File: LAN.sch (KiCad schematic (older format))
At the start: 34 parts, among them J1 Pulse_JXD6-0001NL, U7 LAN8742A-CZ-TR, Y1 NX2016SA-25MHz

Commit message: begin MCU editing
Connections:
- net RMII_CRS_DV: no longer R13.1, R14.1
- new net RMII_RXD0: R13.1
- new net RMII_RXD1: R14.1
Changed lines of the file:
@@
 $Descr A4 11693 8268
 encoding utf-8
-Sheet 2 10
+Sheet 2 9
 Title ""
 Date ""
@@
 Wire Wire Line
 	1130 3590 1380 3590
-Text HLabel 1130 3590 0    50   BiDi ~ 0
-RMII_CRS_DV
 Wire Wire Line
 	1680 3590 2410 3590
@@
 Wire Wire Line
 	1130 3490 1380 3490
-Text HLabel 1130 3490 0    50   BiDi ~ 0
-RMII_CRS_DV
 Wire Wire Line
 	1680 3490 2130 3490
@@
 Wire Wire Line
 	10120 2490 10120 2590
+Text HLabel 1130 3490 0    50   BiDi ~ 0
+RMII_RXD0
+Text HLabel 1130 3590 0    50   BiDi ~ 0
+RMII_RXD1
 $EndSCHEMATC

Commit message: v0.1
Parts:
- added J11: OSTTC020162, digikey-footprints:Term_Block_1x2_P5mm, symbol dk_Terminal-Blocks-Wire-to-Board:OSTTC020162
- renumbered C6 to C86, C7 to C87, C8 to C88, C9 to C89, C10 to C90, C11 to C91, C12 to C92, C13 to C93, C14 to C94, C15 to C95, C16 to C96, D1 to D13, J1 to J10, L2 to L6, R1 to R74, R2 to R75, R3 to R76, R4 to R77, R5 to R78, R6 to R79, R7 to R80, R8 to R81, R9 to R82, R10 to R83, R11 to R84, R12 to R85, R13 to R86, R14 to R87, R15 to R88, R16 to R89, R17 to R90, R18 to R91, U7 to U28, Y1 to Y3
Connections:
- net GNDS: now also J11.1, J11.2

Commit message: v0.3 changed sd_card holder
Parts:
- renumbered C86 to C83, C87 to C84, C88 to C85, C89 to C86, C90 to C87, C91 to C88, C92 to C89, C93 to C90, C94 to C91, C95 to C92, C96 to C93, D13 to D15, J10 to J11, J11 to J12, R74 to R78, R75 to R79, R76 to R80, R77 to R81, R78 to R82, R79 to R83, R80 to R84, R81 to R85, R82 to R86, R83 to R87, R84 to R88, R85 to R89, R86 to R90, R87 to R91, R88 to R92, R89 to R93, R90 to R94, R91 to R95, U28 to U30

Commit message: footprints associations is done
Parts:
- C94: renamed from C92; Type CL10B105KA8NNNC -> GRM188R71H471KA01D
- D15: footprint digikey-footprints:SOT23-6L -> Package_TO_SOT_SMD:SOT-23-6_Handsoldering
- L6: value 600R@100MHz -> 600R@100MHz [BK2125HS601-T]; footprint (none) -> Inductor_SMD:L_0805_2012Metric_Pad1.15x1.40mm_HandSolder
- Y3: footprint (none) -> Crystal:Crystal_SMD_2016-4Pin_2.0x1.6mm
- renumbered C83 to C85, C84 to C86, C85 to C87, C86 to C88, C87 to C89, C88 to C90, C89 to C91, C90 to C92, C91 to C93, C93 to C95, R92 to R100, R93 to R101, R94 to R102, R95 to R103, R78 to R86, R79 to R87, R80 to R88, R81 to R89, R82 to R90, R83 to R91, R84 to R92, R85 to R93, R86 to R94, R87 to R95, R88 to R96, R89 to R97, R90 to R98, R91 to R99
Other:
- moved on the sheet: J12

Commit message: LAN8742 footprint corrected
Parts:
- U30: footprint LAN8742:Microchip-C04-143B-S4QFN-0-0-* -> SVIELCOM:Microchip-C04-143B-S4QFN-0-0-IPC_A
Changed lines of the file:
@@
 F 0 "U30" H 4790 3535 50  0000 C CNN
 F 1 "LAN8742A-CZ-TR" H 4790 3444 50  0000 C CNN
-F 2 "LAN8742:Microchip-C04-143B-S4QFN-0-0-*" H 3290 3670 50  0001 L CNN
+F 2 "SVIELCOM:Microchip-C04-143B-S4QFN-0-0-IPC_A" H 3290 3670 50  0001 L CNN
 F 3 "http://ww1.microchip.com/downloads/en/DeviceDoc/DS_LAN8742_00001989A.pdf" H 3290 3770 50  0001 L CNN
 F 4 "+70°C" H 3290 3870 50  0001 L CNN "ambient temperature range high"

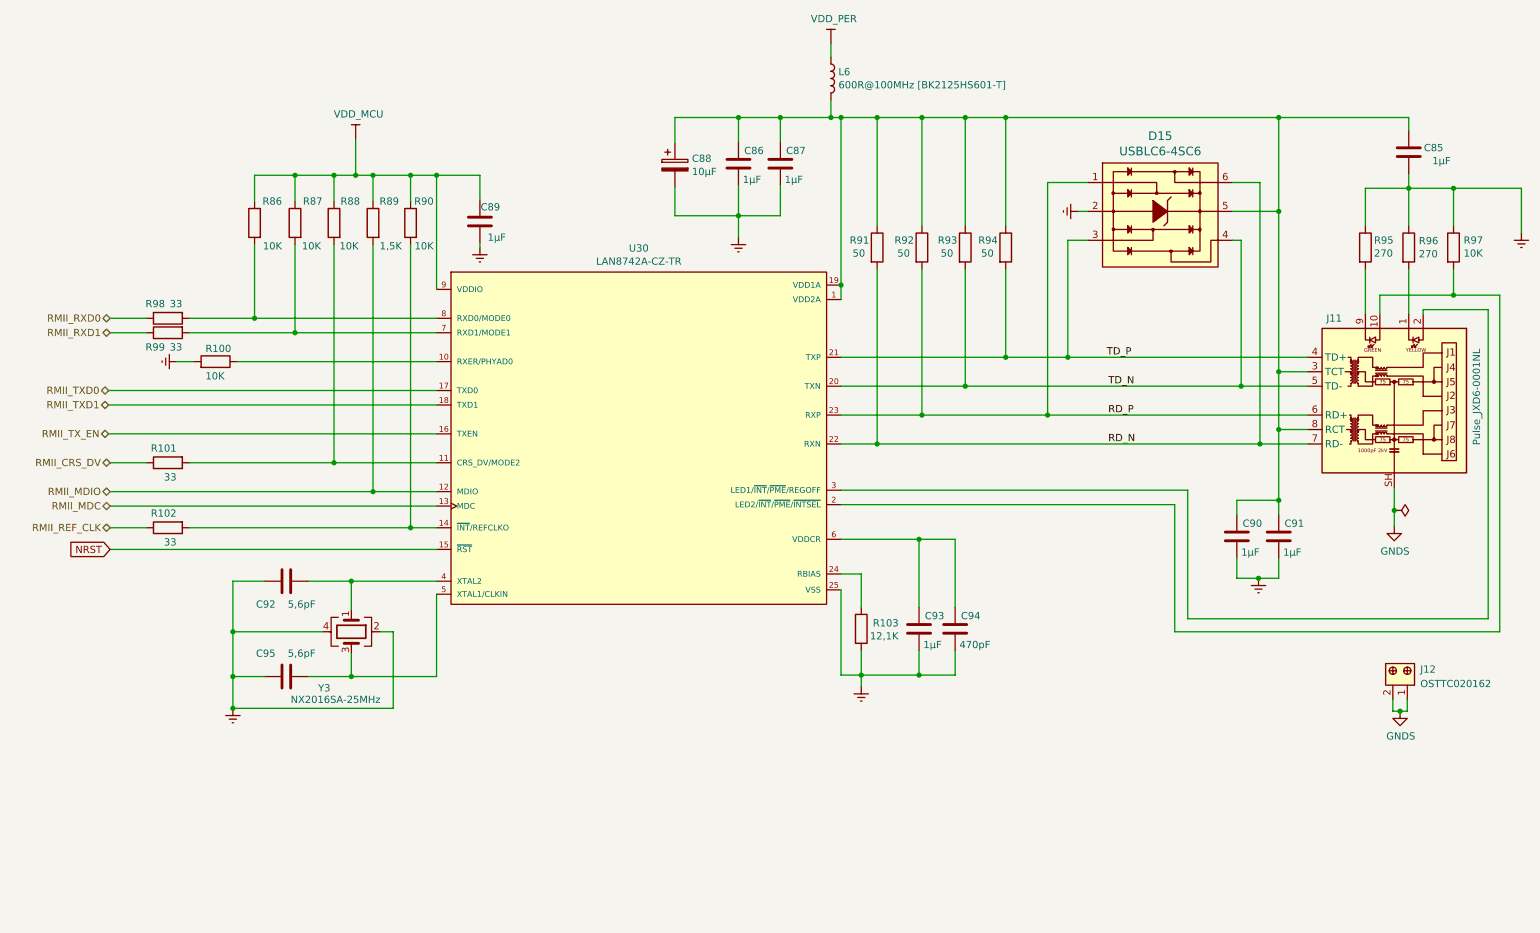
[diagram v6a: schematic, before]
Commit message: corrected few footprints, correct all resistors and capacitors type for ordering
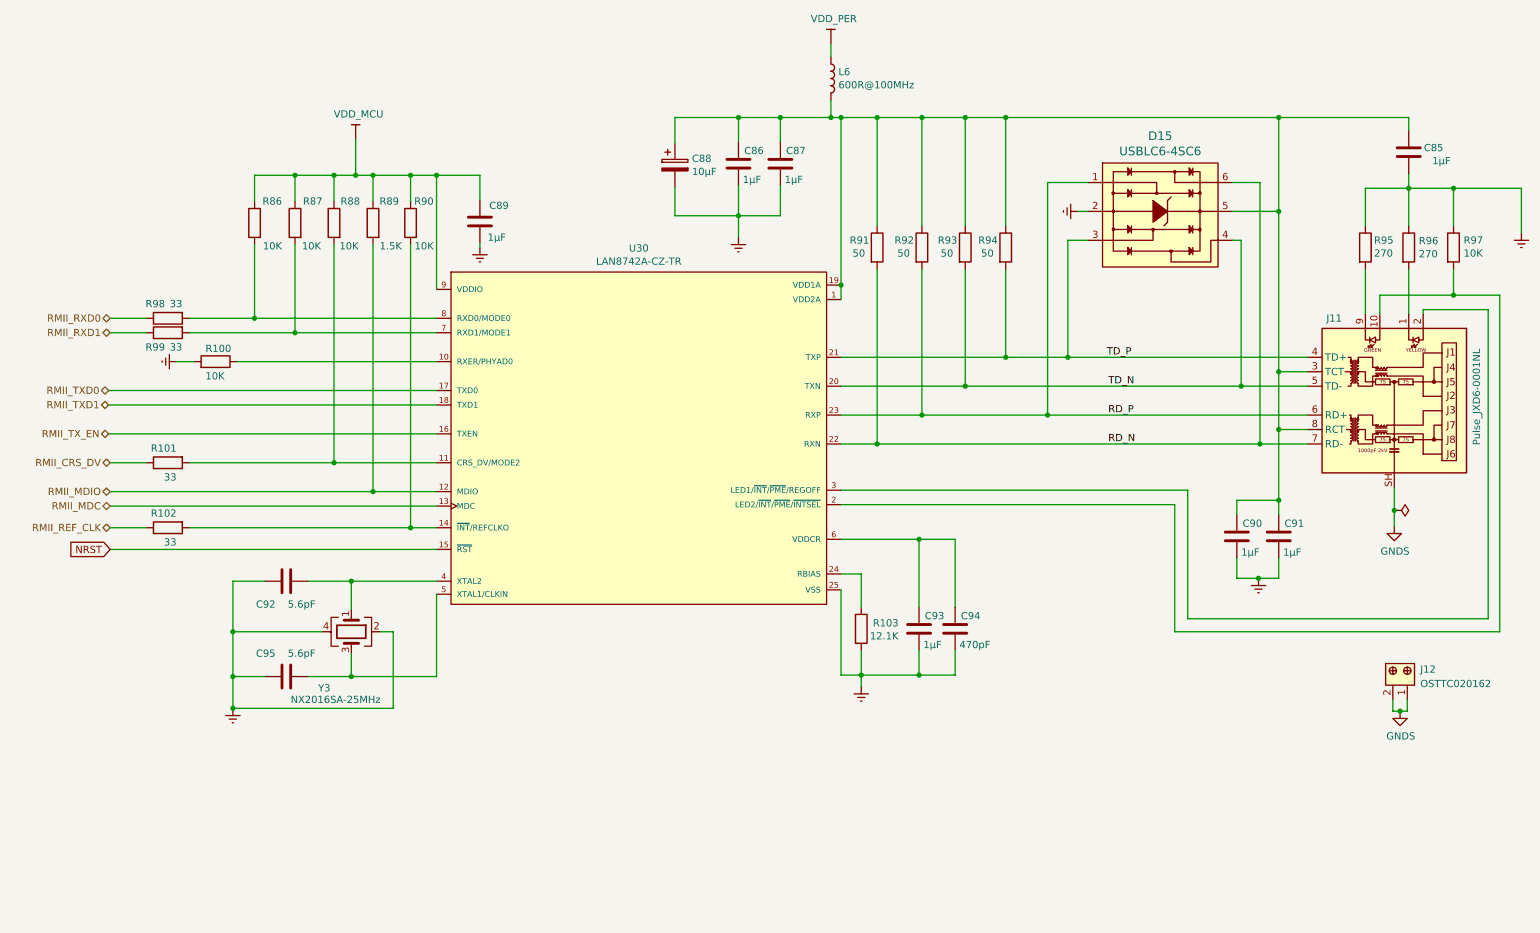
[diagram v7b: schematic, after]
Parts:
- C92, C95: value 5,6pF -> 5.6pF; Type CL10B105KA8NNNC -> CC0603CRNPO9BN5R6
- L6: value 600R@100MHz [BK2125HS601-T] -> 600R@100MHz; Type (none) -> BK2125HS601-T
- R100, R86, R87, R88, R90, R97: Type (none) -> RC0805FR-0710KL
- R101, R102, R98, R99: Type (none) -> RC0805FR-0733RL
- R103: value 12,1K -> 12.1K; Type (none) -> RC0805FR-0712K1L
- R89: value 1,5K -> 1.5K; Type (none) -> RC0805FR-071K5L
- R91, R92, R93, R94: footprint Resistor_SMD:R_0805_2012Metric_Pad1.20x1.40mm_HandSolder -> Resistor_SMD:R_0603_1608Metric_Pad0.98x0.95mm_HandSolder; Type (none) -> CRCW060350R0FKEA
- R95, R96: Type (none) -> RC0805FR-07270RL
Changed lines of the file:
@@
 F 2 "Resistor_SMD:R_0805_2012Metric_Pad1.20x1.40mm_HandSolder" V 10360 3000 50  0001 C CNN
 F 3 "~" H 10430 3000 50  0001 C CNN
+F 4 "RC0805FR-0710KL" H 10430 3000 50  0001 C CNN "Type"
 	1    10430 3000
 	1    0    0    -1
@@
 F 2 "Resistor_SMD:R_0805_2012Metric_Pad1.20x1.40mm_HandSolder" V 10050 3000 50  0001 C CNN
 F 3 "~" H 10120 3000 50  0001 C CNN
+F 4 "RC0805FR-07270RL" H 10120 3000 50  0001 C CNN "Type"
 	1    10120 3000
 	1    0    0    -1
@@
 F 2 "Resistor_SMD:R_0805_2012Metric_Pad1.20x1.40mm_HandSolder" V 9750 3000 50  0001 C CNN
 F 3 "~" H 9820 3000 50  0001 C CNN
+F 4 "RC0805FR-07270RL" H 9820 3000 50  0001 C CNN "Type"
 	1    9820 3000
 	1    0    0    -1
@@
 F 0 "R94" H 7140 3050 50  0000 L CNN
 F 1 "50" H 7160 2960 50  0000 L CNN
-F 2 "Resistor_SMD:R_0805_2012Metric_Pad1.20x1.40mm_HandSolder" V 7260 3000 50  0001 C CNN
+F 2 "Resistor_SMD:R_0603_1608Metric_Pad0.98x0.95mm_HandSolder" V 7260 3000 50  0001 C CNN
 F 3 "~" H 7330 3000 50  0001 C CNN
+F 4 "CRCW060350R0FKEA" H 7330 3000 50  0001 C CNN "Type"
 	1    7330 3000
 	1    0    0    -1
@@
 F 0 "R93" H 6860 3050 50  0000 L CNN
 F 1 "50" H 6880 2960 50  0000 L CNN
-F 2 "Resistor_SMD:R_0805_2012Metric_Pad1.20x1.40mm_HandSolder" V 6980 3000 50  0001 C CNN
+F 2 "Resistor_SMD:R_0603_1608Metric_Pad0.98x0.95mm_HandSolder" V 6980 3000 50  0001 C CNN
 F 3 "~" H 7050 3000 50  0001 C CNN
+F 4 "CRCW060350R0FKEA" H 7050 3000 50  0001 C CNN "Type"
 	1    7050 3000
 	1    0    0    -1
@@
 F 0 "R92" H 6560 3050 50  0000 L CNN
 F 1 "50" H 6580 2960 50  0000 L CNN
-F 2 "Resistor_SMD:R_0805_2012Metric_Pad1.20x1.40mm_HandSolder" V 6680 3000 50  0001 C CNN
+F 2 "Resistor_SMD:R_0603_1608Metric_Pad0.98x0.95mm_HandSolder" V 6680 3000 50  0001 C CNN
 F 3 "~" H 6750 3000 50  0001 C CNN
+F 4 "CRCW060350R0FKEA" H 6750 3000 50  0001 C CNN "Type"
 	1    6750 3000
 	1    0    0    -1
@@
 F 0 "R91" H 6250 3050 50  0000 L CNN
 F 1 "50" H 6270 2960 50  0000 L CNN
-F 2 "Resistor_SMD:R_0805_2012Metric_Pad1.20x1.40mm_HandSolder" V 6370 3000 50  0001 C CNN
+F 2 "Resistor_SMD:R_0603_1608Metric_Pad0.98x0.95mm_HandSolder" V 6370 3000 50  0001 C CNN
 F 3 "~" H 6440 3000 50  0001 C CNN
+F 4 "CRCW060350R0FKEA" H 6440 3000 50  0001 C CNN "Type"
 	1    6440 3000
 	1    0    0    -1
@@
 P 6330 5640
 F 0 "R103" H 6410 5680 50  0000 L CNN
-F 1 "12,1K" H 6390 5590 50  0000 L CNN
+F 1 "12.1K" H 6390 5590 50  0000 L CNN
 F 2 "Resistor_SMD:R_0805_2012Metric_Pad1.20x1.40mm_HandSolder" V 6260 5640 50  0001 C CNN
 F 3 "~" H 6330 5640 50  0001 C CNN
+F 4 "RC0805FR-0712K1L" H 6330 5640 50  0001 C CNN "Type"
 	1    6330 5640
 	1    0    0    -1
@@
 AR Path="/608C7842/6098C4C6" Ref="C95"  Part="1"
 F 0 "C95" V 2190 5760 50  0000 L CNN
-F 1 "5,6pF" V 2190 5980 50  0000 L CNN
+F 1 "5.6pF" V 2190 5980 50  0000 L CNN
 F 2 "Capacitor_SMD:C_0603_1608Metric_Pad1.08x0.95mm_HandSolder" H 2388 5820 50  0001 C CNN
 F 3 "http://www.farnell.com/datasheets/2710676.pdf" H 2350 5970 50  0001 C CNN
-F 4 "CL10B105KA8NNNC" H 2350 5970 50  0001 C CNN "Type"
+F 4 "CC0603CRNPO9BN5R6" H 2350 5970 50  0001 C CNN "Type"
 	1    2350 5970
 	0    1    1    0
@@
 AR Path="/608C7842/6098D1AF" Ref="C92"  Part="1"
 F 0 "C92" V 2510 5100 50  0000 L CNN
-F 1 "5,6pF" V 2510 5320 50  0000 L CNN
+F 1 "5.6pF" V 2510 5320 50  0000 L CNN
 F 2 "Capacitor_SMD:C_0603_1608Metric_Pad1.08x0.95mm_HandSolder" H 2388 5160 50  0001 C CNN
 F 3 "http://www.farnell.com/datasheets/2710676.pdf" H 2350 5310 50  0001 C CNN
-F 4 "CL10B105KA8NNNC" H 2350 5310 50  0001 C CNN "Type"
+F 4 "CC0603CRNPO9BN5R6" H 2350 5310 50  0001 C CNN "Type"
 	1    2350 5310
 	0    1    1    0
@@
 F 2 "Resistor_SMD:R_0805_2012Metric_Pad1.20x1.40mm_HandSolder" V 3140 2830 50  0001 C CNN
 F 3 "~" H 3210 2830 50  0001 C CNN
+F 4 "RC0805FR-0710KL" H 3210 2830 50  0001 C CNN "Type"
 	1    3210 2830
 	-1   0    0    -1
@@
 F 2 "Resistor_SMD:R_0805_2012Metric_Pad1.20x1.40mm_HandSolder" V 1460 4940 50  0001 C CNN
 F 3 "~" H 1530 4940 50  0001 C CNN
+F 4 "RC0805FR-0733RL" V 1530 4940 50  0001 C CNN "Type"
 	1    1530 4940
 	0    -1   1    0
@@
 AR Path="/608C7842/609E3A1C" Ref="L6"  Part="1"
 F 0 "L6" H 6172 1876 50  0000 L CNN
-F 1 "600R@100MHz [BK2125HS601-T]" H 6172 1785 50  0000 L CNN
+F 1 "600R@100MHz" H 6172 1785 50  0000 L CNN
 F 2 "Inductor_SMD:L_0805_2012Metric_Pad1.15x1.40mm_HandSolder" H 6120 1830 50  0001 C CNN
 F 3 "~" H 6120 1830 50  0001 C CNN
+F 4 "BK2125HS601-T" H 6120 1830 50  0001 C CNN "Type"
 	1    6120 1830
 	1    0    0    -1
@@
 AR Path="/60A03F8A/609B2A2A" Ref="C?"  Part="1"
 AR Path="/608C7842/609B2A2A" Ref="C89"  Part="1"
-F 0 "C89" H 3550 2720 50  0000 L CNN
+F 0 "C89" H 3490 2710 50  0000 L CNN
 F 1 "1µF" H 3510 2930 50  0000 L CNN
 F 2 "Capacitor_SMD:C_0603_1608Metric_Pad1.08x0.95mm_HandSolder" H 3728 2670 50  0001 C CNN
@@
 P 2950 2830
 F 0 "R89" H 2770 2980 50  0000 L CNN
-F 1 "1,5K" H 2750 2670 50  0000 L CNN
+F 1 "1.5K" H 2750 2670 50  0000 L CNN
 F 2 "Resistor_SMD:R_0805_2012Metric_Pad1.20x1.40mm_HandSolder" V 2880 2830 50  0001 C CNN
 F 3 "~" H 2950 2830 50  0001 C CNN
+F 4 "RC0805FR-071K5L" H 2950 2830 50  0001 C CNN "Type"
 	1    2950 2830
 	-1   0    0    -1
@@
 F 2 "Resistor_SMD:R_0805_2012Metric_Pad1.20x1.40mm_HandSolder" V 1460 4490 50  0001 C CNN
 F 3 "~" H 1530 4490 50  0001 C CNN
+F 4 "RC0805FR-0733RL" V 1530 4490 50  0001 C CNN "Type"
 	1    1530 4490
 	0    -1   1    0
@@
 F 2 "Resistor_SMD:R_0805_2012Metric_Pad1.20x1.40mm_HandSolder" V 1790 3790 50  0001 C CNN
 F 3 "~" H 1860 3790 50  0001 C CNN
+F 4 "RC0805FR-0710KL" V 1860 3790 50  0001 C CNN "Type"
 	1    1860 3790
 	0    1    -1   0
@@
 F 2 "Resistor_SMD:R_0805_2012Metric_Pad1.20x1.40mm_HandSolder" V 1460 3590 50  0001 C CNN
 F 3 "~" H 1530 3590 50  0001 C CNN
+F 4 "RC0805FR-0733RL" V 1530 3590 50  0001 C CNN "Type"
 	1    1530 3590
 	0    -1   1    0
@@
 F 2 "Resistor_SMD:R_0805_2012Metric_Pad1.20x1.40mm_HandSolder" V 1460 3490 50  0001 C CNN
 F 3 "~" H 1530 3490 50  0001 C CNN
+F 4 "RC0805FR-0733RL" V 1530 3490 50  0001 C CNN "Type"
 	1    1530 3490
 	0    -1   1    0
@@
 F 2 "Resistor_SMD:R_0805_2012Metric_Pad1.20x1.40mm_HandSolder" V 2610 2830 50  0001 C CNN
 F 3 "~" H 2680 2830 50  0001 C CNN
+F 4 "RC0805FR-0710KL" H 2680 2830 50  0001 C CNN "Type"
 	1    2680 2830
 	-1   0    0    -1
@@
 F 2 "Resistor_SMD:R_0805_2012Metric_Pad1.20x1.40mm_HandSolder" V 2340 2830 50  0001 C CNN
 F 3 "~" H 2410 2830 50  0001 C CNN
+F 4 "RC0805FR-0710KL" H 2410 2830 50  0001 C CNN "Type"
 	1    2410 2830
 	-1   0    0    -1
@@
 F 2 "Resistor_SMD:R_0805_2012Metric_Pad1.20x1.40mm_HandSolder" V 2060 2830 50  0001 C CNN
 F 3 "~" H 2130 2830 50  0001 C CNN
+F 4 "RC0805FR-0710KL" H 2130 2830 50  0001 C CNN "Type"
 	1    2130 2830
 	-1   0    0    -1
